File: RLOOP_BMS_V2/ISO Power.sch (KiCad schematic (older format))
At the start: 3 parts, among them U4 MIC5282-5.0YMM

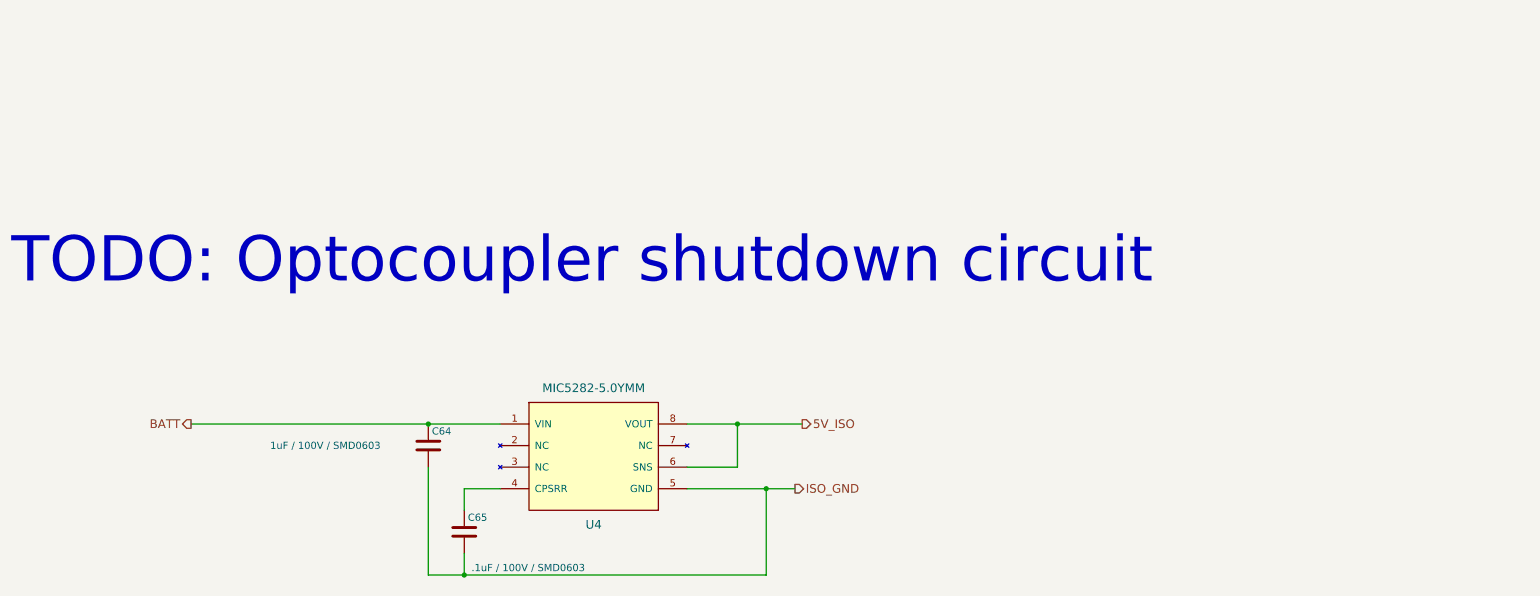
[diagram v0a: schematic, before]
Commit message: more WIP
making room for a thermal pad and power circuits
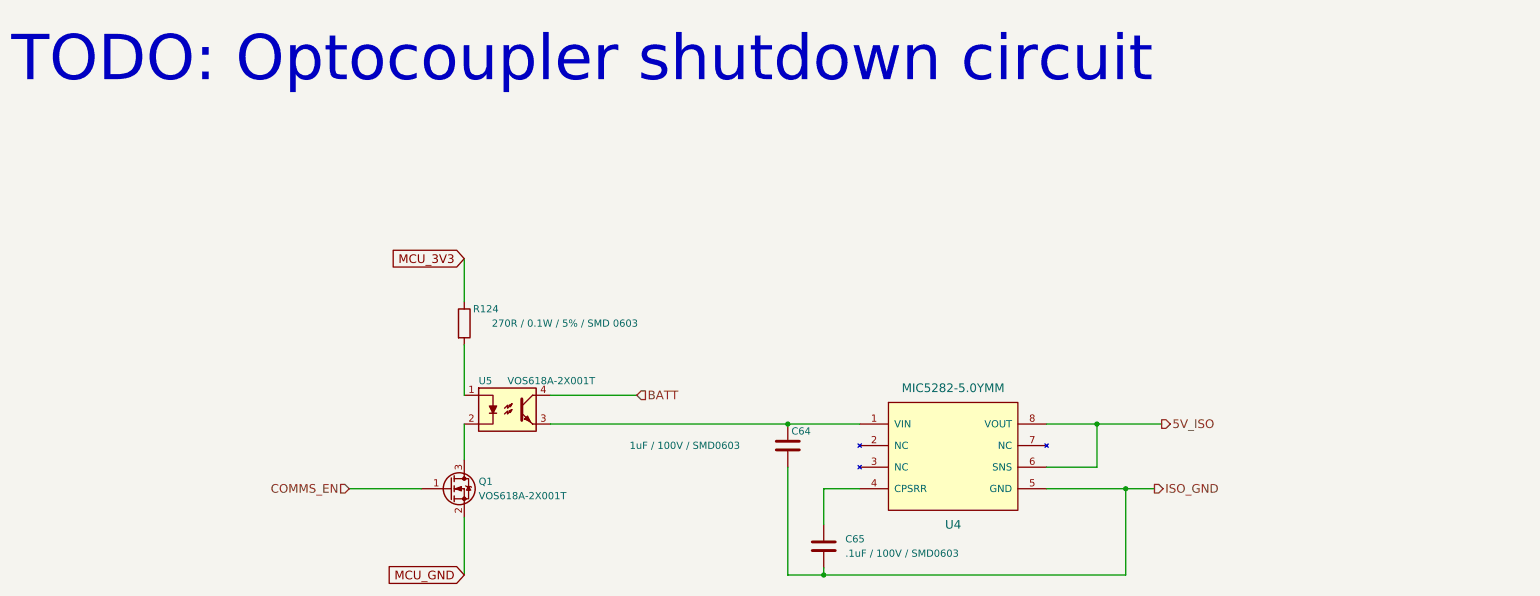
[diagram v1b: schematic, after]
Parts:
- added Q1: VOS618A-2X001T, TO_SOT_Packages_SMD:SuperSOT-3, symbol Q_NMOS_GSD
- added R124: 270R / 0.1W / 5% / SMD 0603, Resistors_SMD:R_0603, symbol R
- added U5: VOS618A-2X001T, rLoop_Footprints:VOS618A-2X001T, symbol LTV-817
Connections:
- net BATT: now also U5.4; no longer C64.1, U4.1 (VIN)
- new net: C64.1, U4.1 (VIN), U5.3
- new net: R124.2, U5.1
- new net: Q1.3 (D), U5.2
- new net COMMS_EN: Q1.1 (G)
- new net MCU_3V3: R124.1
- new net MCU_GND: Q1.2 (S)
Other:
- moved on the sheet: C64, C65, U4
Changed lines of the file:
@@
 L MIC5282-3.3YMM U4
 U 1 1 592F5016
-P 5700 3700
-F 0 "U4" H 5700 3200 60  0000 C CNN
-F 1 "MIC5282-5.0YMM" H 5700 4150 60  0000 C CNN
-F 2 "rLoop_Footprints:MIC5282" H 5450 3700 60  0001 C CNN
-F 3 "" H 5450 3700 60  0001 C CNN
-	1    5700 3700
+P 8200 3700
+F 0 "U4" H 8200 3200 60  0000 C CNN
+F 1 "MIC5282-5.0YMM" H 8200 4150 60  0000 C CNN
+F 2 "rLoop_Footprints:MIC5282" H 7950 3700 60  0001 C CNN
+F 3 "" H 7950 3700 60  0001 C CNN
+	1    8200 3700
 	1    0    0    -1
 $EndComp
@@
 L C C64
 U 1 1 592F506E
-P 4550 3650
-F 0 "C64" H 4575 3750 50  0000 L CNN
-F 1 "1uF / 100V / SMD0603" H 3450 3650 50  0000 L CNN
-F 2 "Capacitors_SMD:C_0603" H 4588 3500 50  0001 C CNN
-F 3 "" H 4550 3650 50  0001 C CNN
-	1    4550 3650
+P 7050 3650
+F 0 "C64" H 7075 3750 50  0000 L CNN
+F 1 "1uF / 100V / SMD0603" H 5950 3650 50  0000 L CNN
+F 2 "Capacitors_SMD:C_0603" H 7088 3500 50  0001 C CNN
+F 3 "" H 7050 3650 50  0001 C CNN
+	1    7050 3650
 	1    0    0    -1
 $EndComp
 Wire Wire Line
-	2900 3500 5050 3500
-Text HLabel 7100 3950 2    60   Output ~ 0
+	5400 3500 7550 3500
+Text HLabel 9600 3950 2    60   Output ~ 0
 ISO_GND
 Wire Wire Line
-	6350 3950 7100 3950
+	8850 3950 9600 3950
 Wire Wire Line
-	4550 3800 4550 4550
+	7050 3800 7050 4550
 Wire Wire Line
-	4550 4550 6900 4550
+	7050 4550 9400 4550
 Wire Wire Line
-	6900 4550 6900 3950
-Connection ~ 6900 3950
+	9400 4550 9400 3950
+Connection ~ 9400 3950
 $Comp
 L C C65
 U 1 1 592F5118
-P 4800 4250
-F 0 "C65" H 4825 4350 50  0000 L CNN
-F 1 ".1uF / 100V / SMD0603" H 4850 4000 50  0000 L CNN
-F 2 "Capacitors_SMD:C_0603" H 4838 4100 50  0001 C CNN
-F 3 "" H 4800 4250 50  0001 C CNN
-	1    4800 4250
+P 7300 4350
+F 0 "C65" H 7450 4400 50  0000 L CNN
+F 1 ".1uF / 100V / SMD0603" H 7450 4300 50  0000 L CNN
+F 2 "Capacitors_SMD:C_0603" H 7338 4200 50  0001 C CNN
+F 3 "" H 7300 4350 50  0001 C CNN
+	1    7300 4350
 	1    0    0    -1
 $EndComp
 Wire Wire Line
-	4800 4400 4800 4550
-Connection ~ 4800 4550
+	7300 4500 7300 4550
+Connection ~ 7300 4550
 Wire Wire Line
-	6350 3500 7150 3500
+	8850 3500 9650 3500
 Wire Wire Line
-	6700 3500 6700 3800
+	9200 3500 9200 3800
 Wire Wire Line
-	6700 3800 6350 3800
-Text HLabel 2900 3500 0    60   Output ~ 0
+	9200 3800 8850 3800
+Text HLabel 6000 3300 2    60   Input ~ 0
 BATT
-Connection ~ 4550 3500
-Text Notes 1650 2550 0    315  ~ 0
+Connection ~ 7050 3500
+Text Notes 1650 1150 0    315  ~ 0
 TODO: Optocoupler shutdown circuit
-Text HLabel 7150 3500 2    60   Output ~ 0
+Text HLabel 9650 3500 2    60   Output ~ 0
 5V_ISO
-Connection ~ 6700 3500
+Connection ~ 9200 3500
 Wire Wire Line
-	5050 3950 4800 3950
+	7550 3950 7300 3950
 Wire Wire Line
-	4800 3950 4800 4100
+	7300 3950 7300 4200
+$Comp
+L LTV-817 U5
+U 1 1 59379A70
+P 5100 3400
+F 0 "U5" H 4900 3600 50  0000 L CNN
+F 1 "VOS618A-2X001T" H 5100 3600 50  0000 L CNN
+F 2 "rLoop_Footprints:VOS618A-2X001T" H 4900 3200 50  0001 L CIN
+F 3 "" H 5100 3300 50  0001 L CNN
+	1    5100 3400
+	1    0    0    -1
+$EndComp
+Wire Wire Line
+	6000 3300 5400 3300
+Text GLabel 4800 2350 0    60   Input ~ 0
+MCU_3V3
+$Comp
+L R R124
+U 1 1 5937A967
+P 4800 2800
+F 0 "R124" H 4950 2900 50  0000 C CNN
+F 1 "270R / 0.1W / 5% / SMD 0603" H 5500 2800 50  0000 C CNN
+F 2 "Resistors_SMD:R_0603" V 4730 2800 50  0001 C CNN
+F 3 "" H 4800 2800 50  0001 C CNN
+	1    4800 2800
+	1    0    0    -1
+$EndComp
+Wire Wire Line
+	4800 2350 4800 2650
+Wire Wire Line
+	4800 2950 4800 3300
+Wire Wire Line
+	4800 3500 4800 3750
+Text GLabel 4800 4550 0    60   Input ~ 0
+MCU_GND
+Wire Wire Line
+	4800 4550 4800 4150
+Text HLabel 4000 3950 0    60   Input ~ 0
+COMMS_EN
+Wire Wire Line
+	4000 3950 4500 3950
+$Comp
+L Q_NMOS_GSD Q1
+U 1 1 5937C31D
+P 4700 3950
+F 0 "Q1" H 4900 4000 50  0000 L CNN
+F 1 "VOS618A-2X001T" H 4900 3900 50  0000 L CNN
+F 2 "TO_SOT_Packages_SMD:SuperSOT-3" H 4900 4050 50  0001 C CNN
+F 3 "" H 4700 3950 50  0001 C CNN
+	1    4700 3950
+	1    0    0    -1
+$EndComp
 $EndSCHEMATC

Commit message: more WIP
TODO:
Fix pin 50
ground planes
figure out GND_2 weirdness
fix optoisolator 3d model
bq IC 3d model
triple check everything
BOM
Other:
- note removed: "TODO: Optocoupler shutdown circuit"
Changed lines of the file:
@@
 BATT
 Connection ~ 7050 3500
-Text Notes 1650 1150 0    315  ~ 0
-TODO: Optocoupler shutdown circuit
 Text HLabel 9650 3500 2    60   Output ~ 0
 5V_ISO

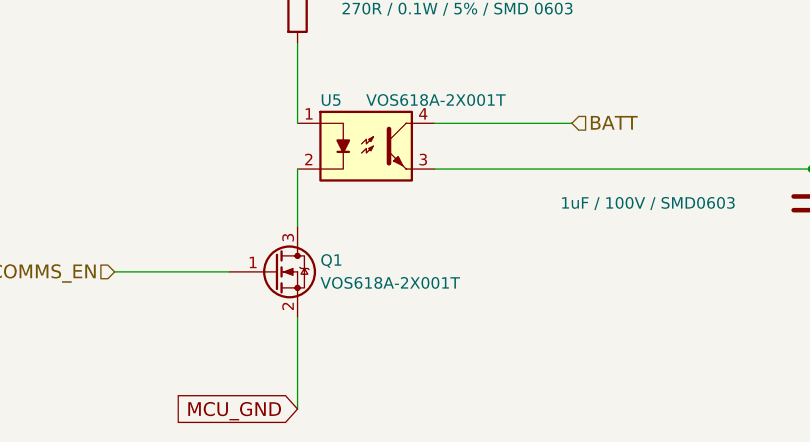
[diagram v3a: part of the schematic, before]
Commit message: Added BOM, added pin 1 markings on a few parts
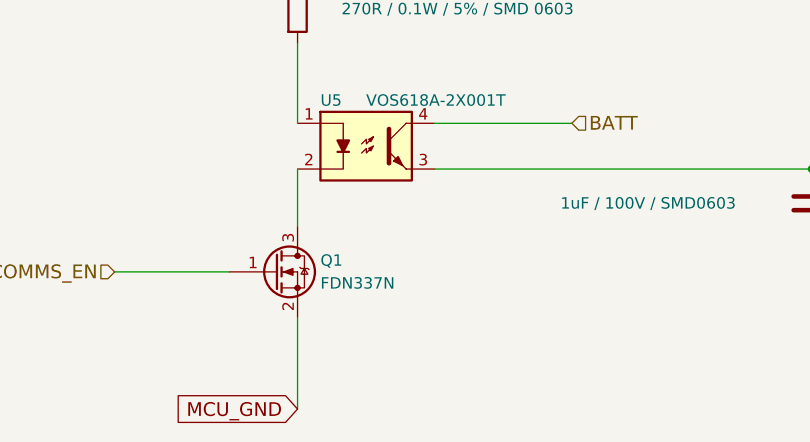
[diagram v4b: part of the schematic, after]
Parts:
- Q1: value VOS618A-2X001T -> FDN337N
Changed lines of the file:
@@
 P 4700 3950
 F 0 "Q1" H 4900 4000 50  0000 L CNN
-F 1 "VOS618A-2X001T" H 4900 3900 50  0000 L CNN
+F 1 "FDN337N" H 4900 3900 50  0000 L CNN
 F 2 "TO_SOT_Packages_SMD:SuperSOT-3" H 4900 4050 50  0001 C CNN
 F 3 "" H 4700 3950 50  0001 C CNN

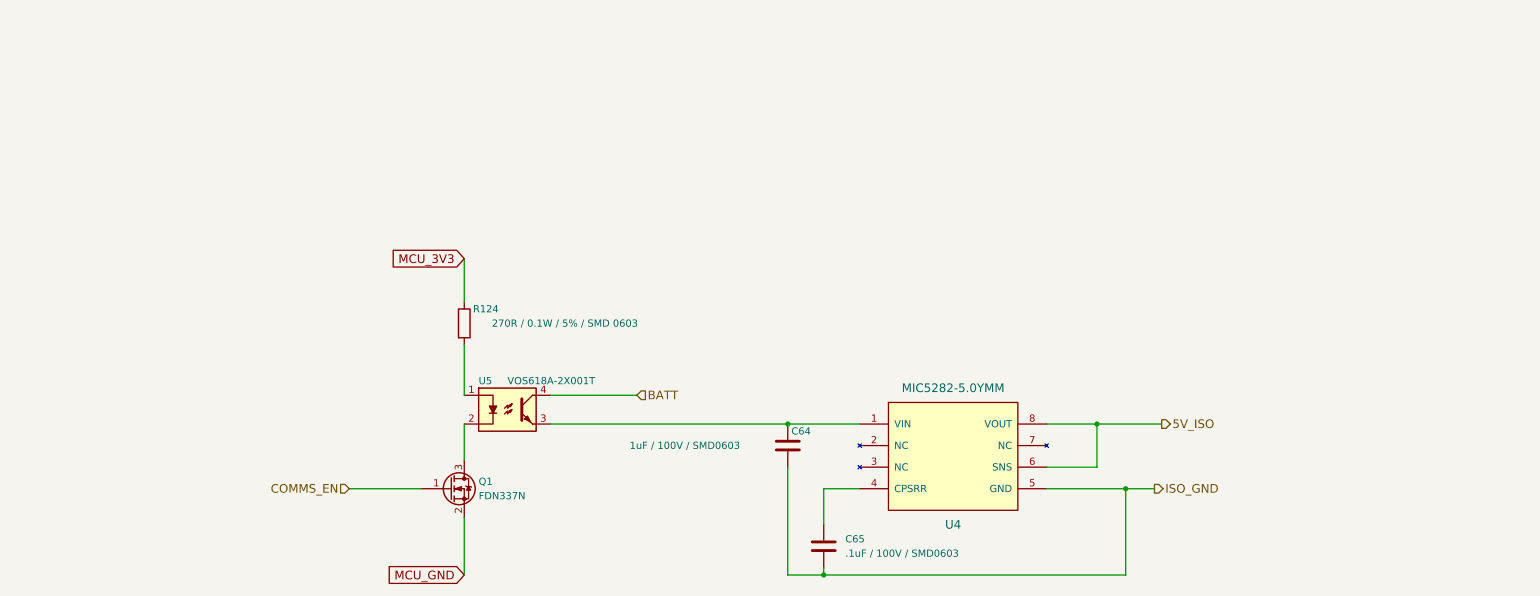
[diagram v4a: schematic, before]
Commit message: Updated page sizes for schematics
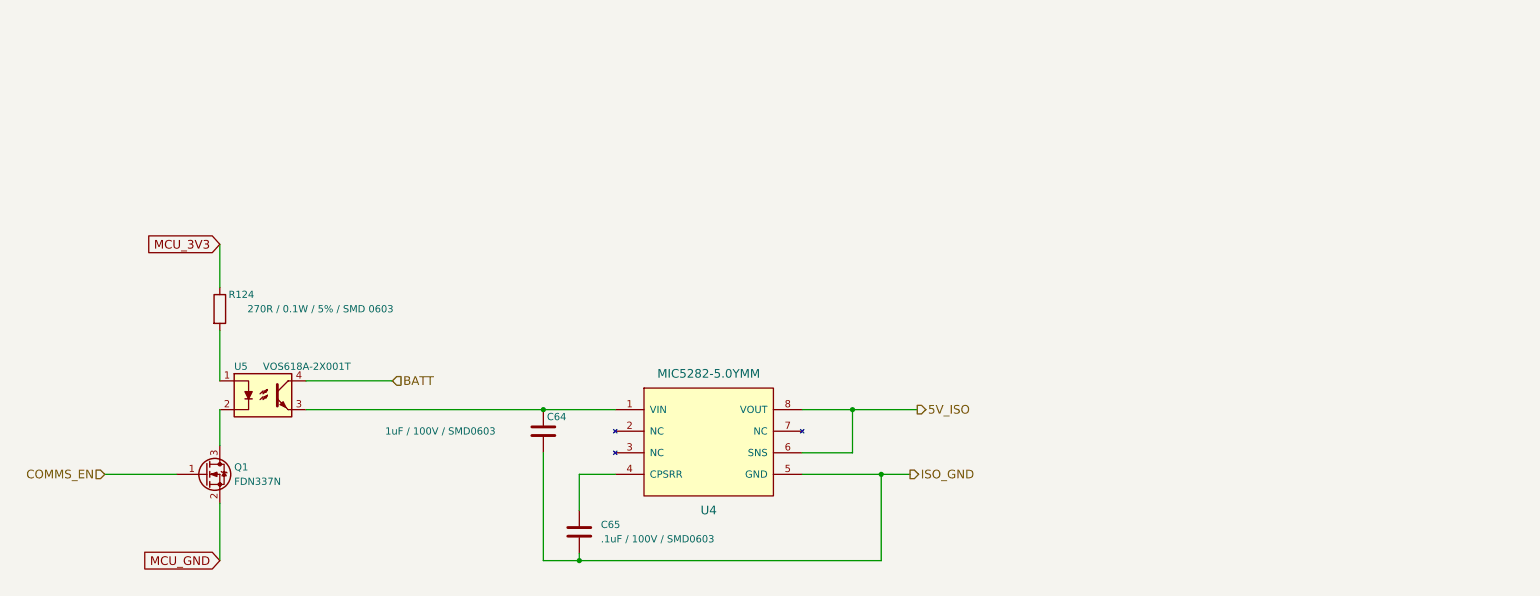
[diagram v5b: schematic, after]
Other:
- moved on the sheet: C64, C65, Q1, R124, U4, U5
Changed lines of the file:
@@
 EELAYER 25 0
 EELAYER END
-$Descr A4 11693 8268
+$Descr USLetter 11000 8500
 encoding utf-8
 Sheet 10 10
@@
 L MIC5282-3.3YMM U4
 U 1 1 592F5016
-P 8200 3700
-F 0 "U4" H 8200 3200 60  0000 C CNN
-F 1 "MIC5282-5.0YMM" H 8200 4150 60  0000 C CNN
-F 2 "rLoop_Footprints:MIC5282" H 7950 3700 60  0001 C CNN
-F 3 "" H 7950 3700 60  0001 C CNN
-	1    8200 3700
+P 6500 3600
+F 0 "U4" H 6500 3100 60  0000 C CNN
+F 1 "MIC5282-5.0YMM" H 6500 4050 60  0000 C CNN
+F 2 "rLoop_Footprints:MIC5282" H 6250 3600 60  0001 C CNN
+F 3 "" H 6250 3600 60  0001 C CNN
+	1    6500 3600
 	1    0    0    -1
 $EndComp
@@
 L C C64
 U 1 1 592F506E
-P 7050 3650
-F 0 "C64" H 7075 3750 50  0000 L CNN
-F 1 "1uF / 100V / SMD0603" H 5950 3650 50  0000 L CNN
-F 2 "Capacitors_SMD:C_0603" H 7088 3500 50  0001 C CNN
-F 3 "" H 7050 3650 50  0001 C CNN
-	1    7050 3650
+P 5350 3550
+F 0 "C64" H 5375 3650 50  0000 L CNN
+F 1 "1uF / 100V / SMD0603" H 4250 3550 50  0000 L CNN
+F 2 "Capacitors_SMD:C_0603" H 5388 3400 50  0001 C CNN
+F 3 "" H 5350 3550 50  0001 C CNN
+	1    5350 3550
 	1    0    0    -1
 $EndComp
 Wire Wire Line
-	5400 3500 7550 3500
-Text HLabel 9600 3950 2    60   Output ~ 0
+	3700 3400 5850 3400
+Text HLabel 7900 3850 2    60   Output ~ 0
 ISO_GND
 Wire Wire Line
-	8850 3950 9600 3950
+	7150 3850 7900 3850
 Wire Wire Line
-	7050 3800 7050 4550
+	5350 3700 5350 4450
 Wire Wire Line
-	7050 4550 9400 4550
+	5350 4450 7700 4450
 Wire Wire Line
-	9400 4550 9400 3950
-Connection ~ 9400 3950
+	7700 4450 7700 3850
+Connection ~ 7700 3850
 $Comp
 L C C65
 U 1 1 592F5118
-P 7300 4350
-F 0 "C65" H 7450 4400 50  0000 L CNN
-F 1 ".1uF / 100V / SMD0603" H 7450 4300 50  0000 L CNN
-F 2 "Capacitors_SMD:C_0603" H 7338 4200 50  0001 C CNN
-F 3 "" H 7300 4350 50  0001 C CNN
-	1    7300 4350
+P 5600 4250
+F 0 "C65" H 5750 4300 50  0000 L CNN
+F 1 ".1uF / 100V / SMD0603" H 5750 4200 50  0000 L CNN
+F 2 "Capacitors_SMD:C_0603" H 5638 4100 50  0001 C CNN
+F 3 "" H 5600 4250 50  0001 C CNN
+	1    5600 4250
 	1    0    0    -1
 $EndComp
 Wire Wire Line
-	7300 4500 7300 4550
-Connection ~ 7300 4550
+	5600 4400 5600 4450
+Connection ~ 5600 4450
 Wire Wire Line
-	8850 3500 9650 3500
+	7150 3400 7950 3400
 Wire Wire Line
-	9200 3500 9200 3800
+	7500 3400 7500 3700
 Wire Wire Line
-	9200 3800 8850 3800
-Text HLabel 6000 3300 2    60   Input ~ 0
+	7500 3700 7150 3700
+Text HLabel 4300 3200 2    60   Input ~ 0
 BATT
-Connection ~ 7050 3500
-Text HLabel 9650 3500 2    60   Output ~ 0
+Connection ~ 5350 3400
+Text HLabel 7950 3400 2    60   Output ~ 0
 5V_ISO
-Connection ~ 9200 3500
+Connection ~ 7500 3400
 Wire Wire Line
-	7550 3950 7300 3950
+	5850 3850 5600 3850
 Wire Wire Line
-	7300 3950 7300 4200
+	5600 3850 5600 4100
 $Comp
 L LTV-817 U5
 U 1 1 59379A70
-P 5100 3400
-F 0 "U5" H 4900 3600 50  0000 L CNN
-F 1 "VOS618A-2X001T" H 5100 3600 50  0000 L CNN
-F 2 "rLoop_Footprints:VOS618A-2X001T" H 4900 3200 50  0001 L CIN
-F 3 "" H 5100 3300 50  0001 L CNN
-	1    5100 3400
+P 3400 3300
+F 0 "U5" H 3200 3500 50  0000 L CNN
+F 1 "VOS618A-2X001T" H 3400 3500 50  0000 L CNN
+F 2 "rLoop_Footprints:VOS618A-2X001T" H 3200 3100 50  0001 L CIN
+F 3 "" H 3400 3200 50  0001 L CNN
+	1    3400 3300
 	1    0    0    -1
 $EndComp
 Wire Wire Line
-	6000 3300 5400 3300
-Text GLabel 4800 2350 0    60   Input ~ 0
+	4300 3200 3700 3200
+Text GLabel 3100 2250 0    60   Input ~ 0
 MCU_3V3
 $Comp
 L R R124
 U 1 1 5937A967
-P 4800 2800
-F 0 "R124" H 4950 2900 50  0000 C CNN
-F 1 "270R / 0.1W / 5% / SMD 0603" H 5500 2800 50  0000 C CNN
-F 2 "Resistors_SMD:R_0603" V 4730 2800 50  0001 C CNN
-F 3 "" H 4800 2800 50  0001 C CNN
-	1    4800 2800
+P 3100 2700
+F 0 "R124" H 3250 2800 50  0000 C CNN
+F 1 "270R / 0.1W / 5% / SMD 0603" H 3800 2700 50  0000 C CNN
+F 2 "Resistors_SMD:R_0603" V 3030 2700 50  0001 C CNN
+F 3 "" H 3100 2700 50  0001 C CNN
+	1    3100 2700
 	1    0    0    -1
 $EndComp
 Wire Wire Line
-	4800 2350 4800 2650
+	3100 2250 3100 2550
 Wire Wire Line
-	4800 2950 4800 3300
+	3100 2850 3100 3200
 Wire Wire Line
-	4800 3500 4800 3750
-Text GLabel 4800 4550 0    60   Input ~ 0
+	3100 3400 3100 3650
+Text GLabel 3100 4450 0    60   Input ~ 0
 MCU_GND
 Wire Wire Line
-	4800 4550 4800 4150
-Text HLabel 4000 3950 0    60   Input ~ 0
+	3100 4450 3100 4050
+Text HLabel 2300 3850 0    60   Input ~ 0
 COMMS_EN
 Wire Wire Line
-	4000 3950 4500 3950
+	2300 3850 2800 3850
 $Comp
 L Q_NMOS_GSD Q1
 U 1 1 5937C31D
-P 4700 3950
-F 0 "Q1" H 4900 4000 50  0000 L CNN
-F 1 "FDN337N" H 4900 3900 50  0000 L CNN
-F 2 "TO_SOT_Packages_SMD:SuperSOT-3" H 4900 4050 50  0001 C CNN
-F 3 "" H 4700 3950 50  0001 C CNN
-	1    4700 3950
+P 3000 3850
+F 0 "Q1" H 3200 3900 50  0000 L CNN
+F 1 "FDN337N" H 3200 3800 50  0000 L CNN
+F 2 "TO_SOT_Packages_SMD:SuperSOT-3" H 3200 3950 50  0001 C CNN
+F 3 "" H 3000 3850 50  0001 C CNN
+	1    3000 3850
 	1    0    0    -1
 $EndComp

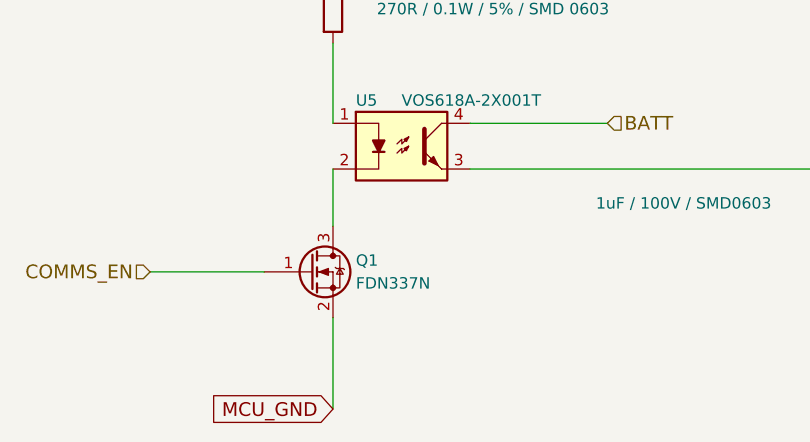
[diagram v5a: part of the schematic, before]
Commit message: change Q1 transistor
Fixing something out of stock
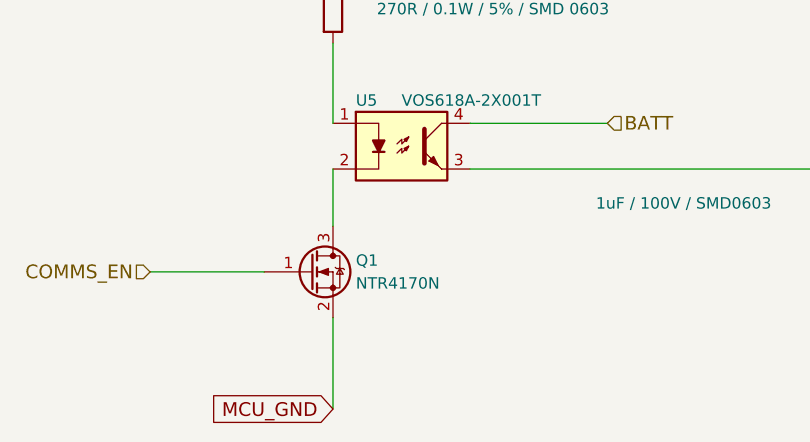
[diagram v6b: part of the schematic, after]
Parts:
- Q1: value FDN337N -> NTR4170N
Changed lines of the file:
@@
 P 3000 3850
 F 0 "Q1" H 3200 3900 50  0000 L CNN
-F 1 "FDN337N" H 3200 3800 50  0000 L CNN
+F 1 "NTR4170N" H 3200 3800 50  0000 L CNN
 F 2 "TO_SOT_Packages_SMD:SuperSOT-3" H 3200 3950 50  0001 C CNN
 F 3 "" H 3000 3850 50  0001 C CNN
